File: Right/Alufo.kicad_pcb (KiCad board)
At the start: 2 copper layers, 139.7 x 88.9 mm, 67 parts, among them J2 USB_C_Receptacle_USB2.0_16P_2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, J4 USB_C_Receptacle_USB2.0_16P_2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, K11 PG1350, K12 PG1350, K13 PG1350, K14 PG1350, K15 PG1350, K16 PG1350, K21 PG1350, K22 PG1350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

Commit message: Manually add cutouts for 2010 resistors
Using middle-layer cutouts defined in the footprint no longer works as the resistors are now vertically aligned in relation to each rather than a set distance from the switch sockets.
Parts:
- R11, R12, R13, R14, R15: footprint Project Library:R_2010_5025Metric_Mod -> Resistor_SMD:R_2010_5025Metric
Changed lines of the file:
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@@
 		)
 	)
-	(footprint "Project Library:R_2010_5025Metric_Mod"
+	(footprint "Resistor_SMD:R_2010_5025Metric"
 		(layer "F.Cu")
 		(at 189.22 54.291679 -90)
@@
 		(tags "resistor")
 		(property "Reference" "R12"
-			(at 0 0 90)
+			(at 0 0 -90)
 			(layer "F.SilkS")
 			(effects
@@
 		)
 		(property "Value" "0R"
-			(at 0 2.28 90)
+			(at 0 2.28 -90)
 			(layer "F.Fab")
 			(effects
@@
 			)
 		)
-		(property "Footprint" "Project Library:R_2010_5025Metric_Mod"
+		(property "Footprint" "Resistor_SMD:R_2010_5025Metric"
 			(at 0 0 -90)
 			(unlocked yes)
@@
 			(layer "F.Fab")
 		)
-		(fp_rect
-			(start -9 -1.825)
-			(end 9 1.825)
-			(stroke
-				(width 0.1)
-				(type default)
-			)
-			(fill none)
-			(layer "User.1")
-		)
 		(fp_text user "${REFERENCE}"
-			(at 0 0 90)
+			(at 0 0 -90)
 			(layer "F.Fab")
 			(effects
@@
 		)
 	)
-	(footprint "Project Library:R_2010_5025Metric_Mod"
+	(footprint "Resistor_SMD:R_2010_5025Metric"
 		(layer "F.Cu")
 		(at 132.07 54.291679 -90)
@@
 			)
 		)
-		(property "Footprint" "Project Library:R_2010_5025Metric_Mod"
+		(property "Footprint" "Resistor_SMD:R_2010_5025Metric"
 			(at 0 0 -90)
 			(unlocked yes)
@@
 			(layer "F.Fab")
 		)
-		(fp_rect
-			(start -9 -1.825)
-			(end 9 1.825)
-			(stroke
-				(width 0.1)
-				(type default)
-			)
-			(fill none)
-			(layer "User.1")
-		)
 		(fp_text user "${REFERENCE}"
 			(at 0 0 -90)
@@
 		)
 	)
-	(footprint "Project Library:R_2010_5025Metric_Mod"
+	(footprint "Resistor_SMD:R_2010_5025Metric"
 		(layer "F.Cu")
 		(at 205.525 64.666681 -90)
@@
 			)
 		)
-		(property "Footprint" "Project Library:R_2010_5025Metric_Mod"
+		(property "Footprint" "Resistor_SMD:R_2010_5025Metric"
 			(at 0 0 -90)
 			(unlocked yes)
@@
 			(layer "F.Fab")
 		)
-		(fp_rect
-			(start -9 -1.825)
-			(end 9 1.825)
-			(stroke
-				(width 0.1)
-				(type default)
-			)
-			(fill none)
-			(layer "User.1")
-		)
 		(fp_text user "${REFERENCE}"
 			(at 0 0 -90)
@@
 		)
 	)
-	(footprint "Project Library:R_2010_5025Metric_Mod"
+	(footprint "Resistor_SMD:R_2010_5025Metric"
 		(layer "F.Cu")
 		(at 170.17 54.291679 -90)
@@
 			)
 		)
-		(property "Footprint" "Project Library:R_2010_5025Metric_Mod"
+		(property "Footprint" "Resistor_SMD:R_2010_5025Metric"
 			(at 0 0 -90)
 			(unlocked yes)
@@
 			(layer "F.Fab")
 		)
-		(fp_rect
-			(start -9 -1.825)
-			(end 9 1.825)
-			(stroke
-				(width 0.1)
-				(type default)
-			)
-			(fill none)
-			(layer "User.1")
-		)
 		(fp_text user "${REFERENCE}"
 			(at 0 0 -90)
@@
 		)
 	)
-	(footprint "Project Library:R_2010_5025Metric_Mod"
+	(footprint "Resistor_SMD:R_2010_5025Metric"
 		(layer "F.Cu")
 		(at 151.12 54.291679 -90)
@@
 			)
 		)
-		(property "Footprint" "Project Library:R_2010_5025Metric_Mod"
+		(property "Footprint" "Resistor_SMD:R_2010_5025Metric"
 			(at 0 0 -90)
 			(unlocked yes)
@@
 			(layer "F.Fab")
 		)
-		(fp_rect
-			(start -9 -1.825)
-			(end 9 1.825)
-			(stroke
-				(width 0.1)
-				(type default)
-			)
-			(fill none)
-			(layer "User.1")
-		)
 		(fp_text user "${REFERENCE}"
 			(at 0 0 -90)
@@
 		(layer "Edge.Cuts")
 	)
+	(gr_rect
+		(start 149.295 43.416676)
+		(end 152.945 60.41668)
+		(stroke
+			(width 0.1)
+			(type default)
+		)
+		(fill none)
+		(layer "User.1")
+	)
+	(gr_rect
+		(start 203.7 56.166679)
+		(end 207.35 73.166683)
+		(stroke
+			(width 0.1)
+			(type default)
+		)
+		(fill none)
+		(layer "User.1")
+	)
+	(gr_rect
+		(start 130.245 47.666677)
+		(end 133.895 57.785)
+		(stroke
+			(width 0.1)
+			(type default)
+		)
+		(fill none)
+		(layer "User.1")
+	)
+	(gr_rect
+		(start 168.345 50.8)
+		(end 171.995 60.41668)
+		(stroke
+			(width 0.1)
+			(type default)
+		)
+		(fill none)
+		(layer "User.1")
+	)
 	(gr_poly
 		(pts
@@
 		)
 		(fill none)
+		(layer "User.1")
+	)
+	(gr_rect
+		(start 187.395 47.666677)
+		(end 191.045 64.666681)
+		(stroke
+			(width 0.1)
+			(type default)
+		)
+		(fill none)

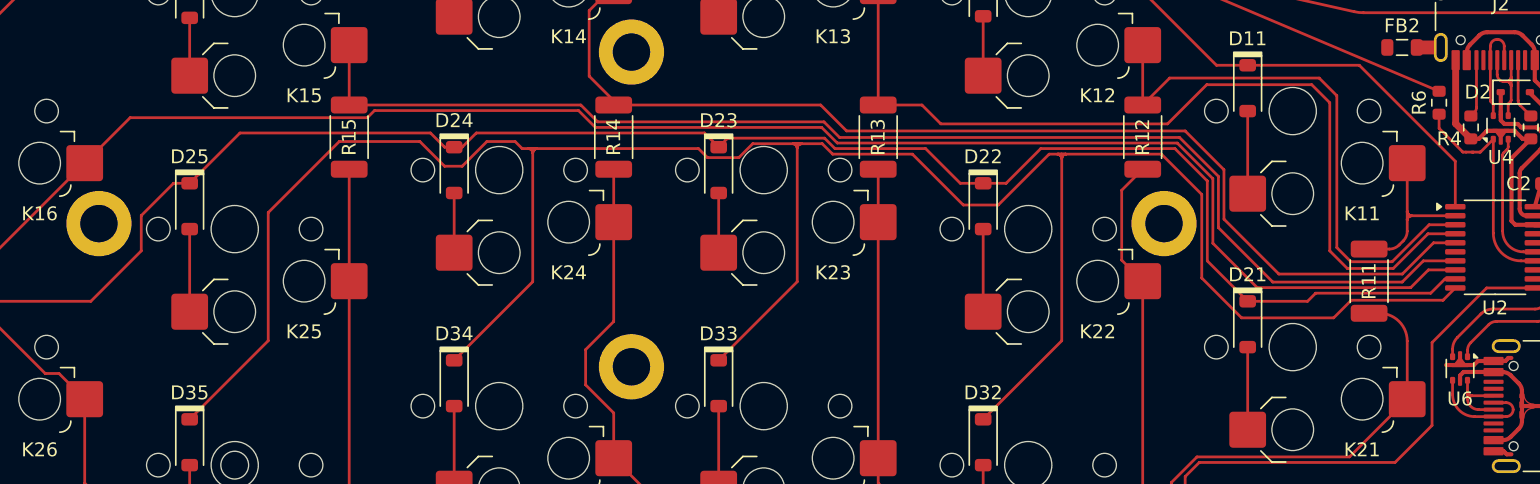
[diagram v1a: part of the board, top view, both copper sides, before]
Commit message: Clean up routing through jumper resistors
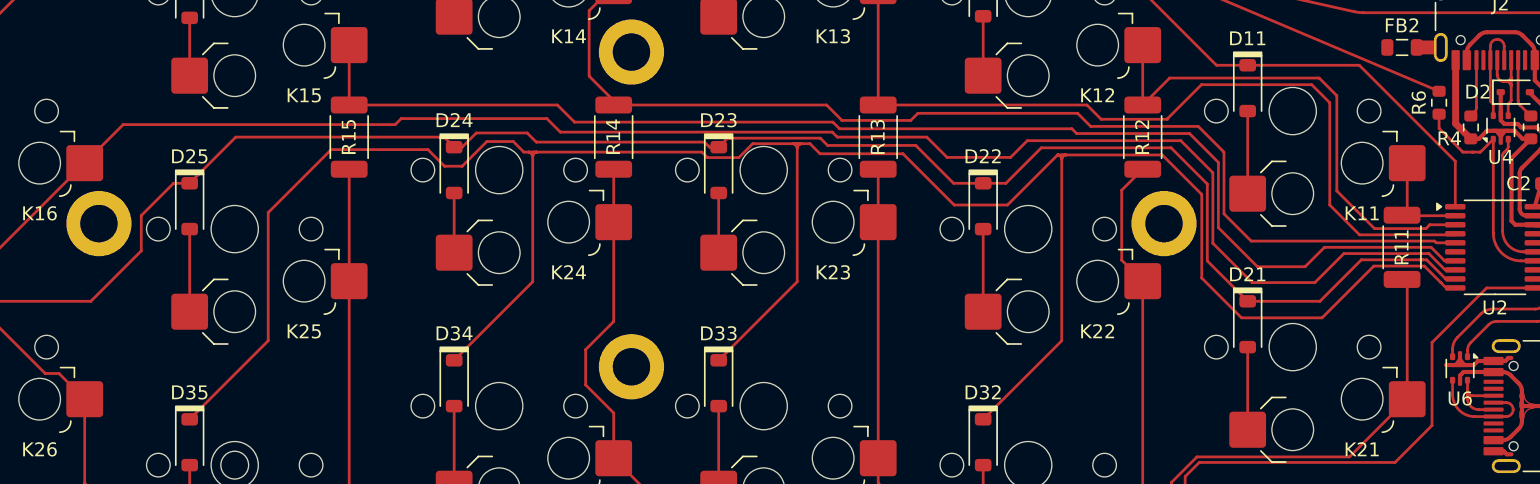
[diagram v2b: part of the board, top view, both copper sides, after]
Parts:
- moved R11 3.40 mm to (207.9, 62.2)
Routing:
- net Col2: track 40.6 -> 36.3 mm
- net Col3: track 64.6 -> 60.4 mm
- net Col1: track 10.9 -> 7.93 mm
- net Col6: track 249.6 -> 251.0 mm
- net Col1T: track 80.8 -> 82.2 mm
- net Row2: track 129.2 -> 130.3 mm
- net Col4: track 78.4 -> 77.5 mm
- net Row3: track 176.8 -> 176.2 mm

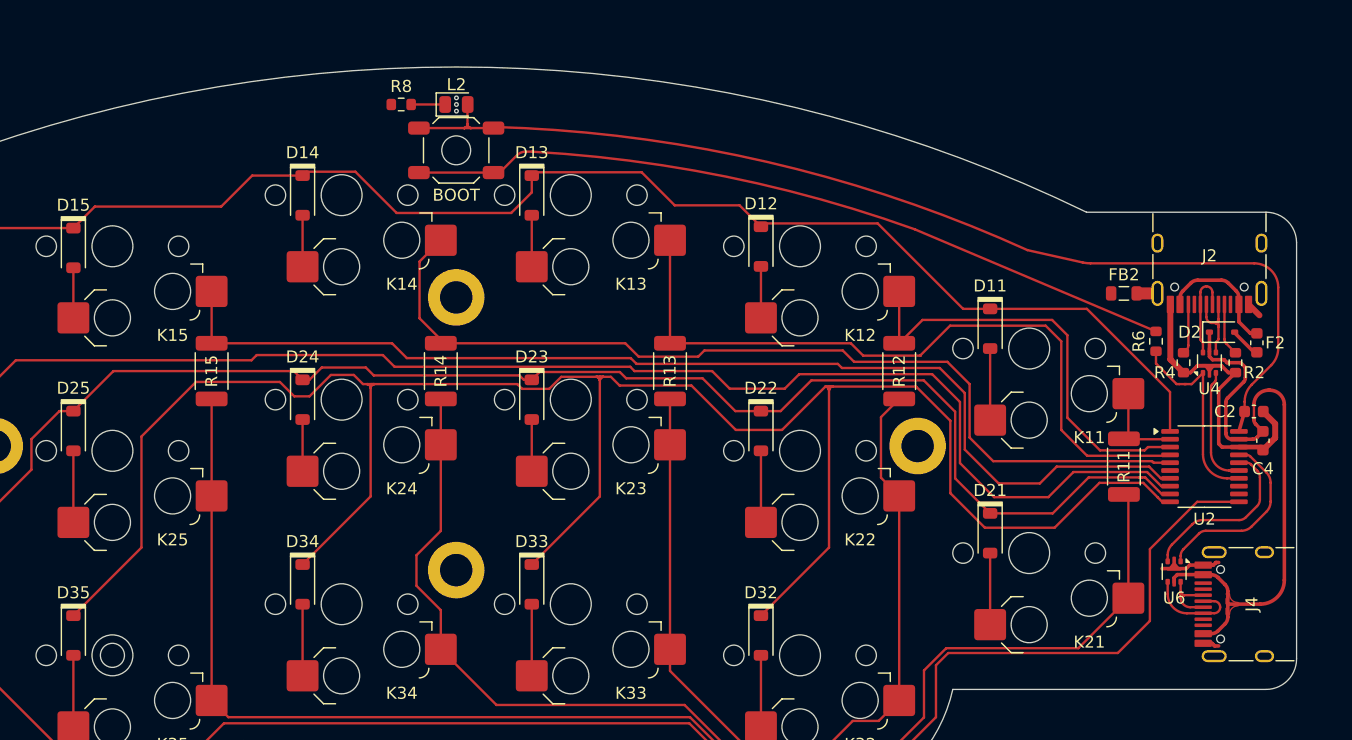
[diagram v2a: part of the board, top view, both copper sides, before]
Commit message: Move boot switch and tweak location of power LED
Boot switch is now closer to the MCU, roughly where the LED would be on the switches K15 (lefthand) or K12 (righthand). The power LED is now a little further away from the top edge.
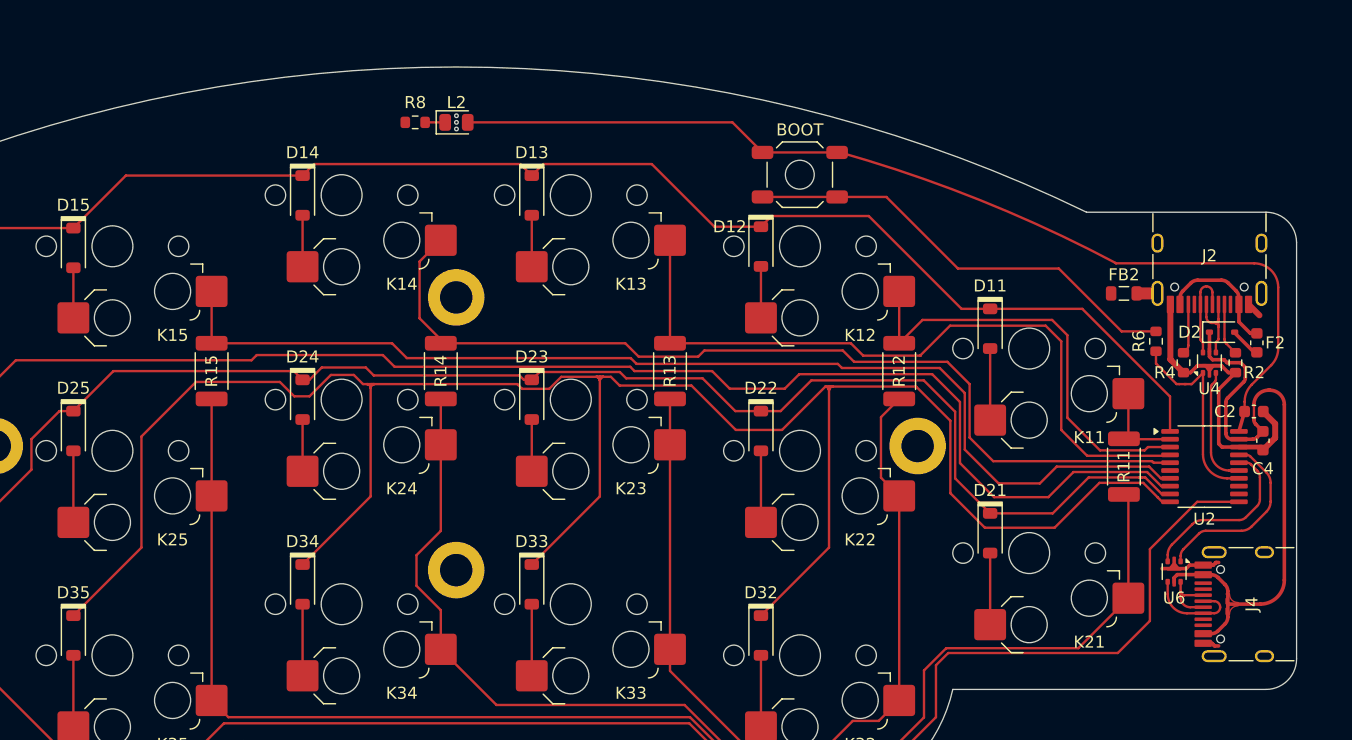
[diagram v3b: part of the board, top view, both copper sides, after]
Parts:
- moved SW2 28.6 mm to (181.0, 38.0)
- moved R8 1.89 mm to (149.0, 33.6)
- moved L2 1.49 mm to (152.4, 33.6)
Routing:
- net +3V3: track 42.3 -> 59.3 mm
- net BOOT: track 31.4 -> 37.3 mm
- net Net-(L2-K): track 2.96 -> 1.67 mm
- net Row1: track 129.1 -> 127.9 mm
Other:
- outline, holes or cut-outs redrawn

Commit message: Clean up routing of right thumb keys
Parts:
- moved D43 0.30 mm to (197.6, 100.7)
- moved D44 0.30 mm to (195.2, 100.2)
- moved D41 0.30 mm to (202.6, 101.6)
- moved D46 0.30 mm to (190.4, 99.2)
- moved D45 0.30 mm to (192.8, 99.7)
- moved D42 0.30 mm to (200.1, 101.1)
- renumbered D46 to D42, D42 to D43, D43 to D44, D44 to D46
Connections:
- D42 pad 1: Net-(D46-K) -> Net-(D42-K)
- D42 pad 2: Col6 -> Col2T
- D43 pad 1: Net-(D42-K) -> Net-(D43-K)
- D43 pad 2: Col2T -> Col3T
- D44 pad 1: Net-(D43-K) -> Net-(D44-K)
- D44 pad 2: Col3T -> Col4T
- D46 pad 1: Net-(D44-K) -> Net-(D46-K)
- D46 pad 2: Col4T -> Col6
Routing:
- net Net-(D46-K): track 40.5 -> 28.4 mm
- net Col6: track 251.0 -> 239.5 mm
- net Row4: track 172.3 -> 164.1 mm
- net Net-(D44-K): track 26.9 -> 32.4 mm
- net Col4T: track 72.8 -> 77.5 mm
- net Net-(D42-K): track 18.0 -> 22.1 mm
- net Col3T: track 58.2 -> 61.0 mm
- net Net-(D43-K): track 18.6 -> 17.4 mm
- net Col5T: track 96.0 -> 95.0 mm
- net Col2T: track 62.8 -> 63.4 mm

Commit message: Clean-up traces on righthand board
Also make tweaks to lefthand
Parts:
- moved NT2 0.26 mm to (212.7, 55.4)
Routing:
- net +3V3: track 59.3 -> 84.0 mm
- net Row3: track 176.2 -> 186.0 mm
- net Row1: track 127.9 -> 123.9 mm
- net Col1T: track 82.5 -> 79.6 mm
- net Row4: track 164.1 -> 161.3 mm
- net BOOT: track 37.3 -> 35.2 mm
- net Col5T: track 95.0 -> 93.5 mm
- net Col4T: track 77.5 -> 76.1 mm
- net Col5: track 92.5 -> 93.9 mm
- net Net-(D42-K): track 22.1 -> 20.7 mm
- net Col2T: track 63.4 -> 62.2 mm
- net Row2: track 130.3 -> 129.3 mm
- net Col3T: track 61.0 -> 60.0 mm

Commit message: Minor tweaks
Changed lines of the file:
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@@
-	)
-	(segment
-		(start 215.408 53.344008)
-		(end 216.23265 53.344008)
-		(width 0.3)
-		(layer "F.Cu")
-		(net 21)
-	)
-	(segment
-		(start 216.7144 59.955)
-		(end 216.8705 59.955)
-		(width 0.3)
-		(layer "F.Cu")
-		(net 21)
 	)
 	(segment
@@
 	)
 	(segment
-		(start 216.23265 53.344008)
-		(end 216.424064 53.535422)
-		(width 0.3)
-		(layer "F.Cu")
-		(net 21)
-	)
-	(segment
 		(start 215.722315 71.450999)
 		(end 216.300686 72.02937)
@@
 		(start 212.074 71.882)
 		(end 212.074 71.464344)
-		(width 0.3)
-		(layer "F.Cu")
-		(net 21)
-	)
-	(segment
-		(start 216.424064 53.535422)
-		(end 217.54478 53.535422)
 		(width 0.3)
 		(layer "F.Cu")
@@
 	)
 	(segment
+		(start 216.506907 53.535422)
+		(end 217.337673 53.535422)
+		(width 0.3)
+		(layer "F.Cu")
+		(net 21)
+	)
+	(segment
+		(start 217.691227 53.681869)
+		(end 217.848554 53.839196)
+		(width 0.3)
+		(layer "F.Cu")
+		(net 21)
+	)
+	(segment
+		(start 216.291229 53.402587)
+		(end 216.365486 53.476844)
+		(width 0.3)
+		(layer "F.Cu")
+		(net 21)
+	)
+	(segment
+		(start 218.705999 58.347892)
+		(end 218.705999 58.166)
+		(width 0.3)
+		(layer "F.Cu")
+		(net 21)
+	)
+	(segment
+		(start 216.300685 75.303999)
+		(end 215.722314 75.88237)
+		(width 0.3)
+		(layer "F.Cu")
+		(net 21)
+	)
+	(segment
+		(start 219.905999 55.88)
+		(end 220.034 55.88)
+		(width 0.3)
+		(layer "F.Cu")
+		(net 21)
+	)
+	(segment
+		(start 217.458 59.955)
+		(end 218.598893 59.955)
+		(width 0.3)
+		(layer "F.Cu")
+		(net 21)
+	)
+	(segment
+		(start 217.995 54.192749)
+		(end 217.995 54.991376)
+		(width 0.3)
+		(layer "F.Cu")
+		(net 21)
+	)
+	(segment
+		(start 215.408 53.344008)
+		(end 216.149807 53.344008)
+		(width 0.3)
+		(layer "F.Cu")
+		(net 21)
+	)
+	(segment
+		(start 216.3705 57.03009)
+		(end 216.3705 59.403993)
+		(width 0.3)
+		(layer "F.Cu")
+		(net 21)
+	)
+	(segment
+		(start 216.516947 59.757547)
+		(end 216.567954 59.808554)
+		(width 0.3)
+		(layer "F.Cu")
+		(net 21)
+	)
+	(segment
+		(start 217.848553 55.34493)
+		(end 216.516946 56.676537)
+		(width 0.3)
+		(layer "F.Cu")
+		(net 21)
+	)
+	(segment
+		(start 216.921507 59.955)
+		(end 217.458 59.955)
+		(width 0.3)
+		(layer "F.Cu")
+		(net 21)
+	)
+	(segment
 		(start 215.008 52.669)
 		(end 215.008 52.944008)
-		(width 0.3)
-		(layer "F.Cu")
-		(net 21)
-	)
-	(segment
-		(start 218.705999 58.347892)
-		(end 218.705999 58.166)
-		(width 0.3)
-		(layer "F.Cu")
-		(net 21)
-	)
-	(segment
-		(start 216.300685 75.303999)
-		(end 215.722314 75.88237)
-		(width 0.3)
-		(layer "F.Cu")
-		(net 21)
-	)
-	(segment
-		(start 217.54478 53.535422)
-		(end 217.995 53.985642)
-		(width 0.3)
-		(layer "F.Cu")
-		(net 21)
-	)
-	(segment
-		(start 216.3705 56.822983)
-		(end 216.3705 59.6111)
-		(width 0.3)
-		(layer "F.Cu")
-		(net 21)
-	)
-	(segment
-		(start 216.3705 59.6111)
-		(end 216.7144 59.955)
-		(width 0.3)
-		(layer "F.Cu")
-		(net 21)
-	)
-	(segment
-		(start 217.995 53.985642)
-		(end 217.995 55.198483)
-		(width 0.3)
-		(layer "F.Cu")
-		(net 21)
-	)
-	(segment
-		(start 219.905999 55.88)
-		(end 220.034 55.88)
-		(width 0.3)
-		(layer "F.Cu")
-		(net 21)
-	)
-	(segment
-		(start 217.458 59.955)
-		(end 218.598893 59.955)
-		(width 0.3)
-		(layer "F.Cu")
-		(net 21)
-	)
-	(segment
-		(start 217.995 55.198483)
-		(end 216.3705 56.822983)
 		(width 0.3)
 		(layer "F.Cu")
@@
 	)
 	(arc
+		(start 216.365486 53.476844)
+		(mid 216.430371 53.520198)
+		(end 216.506907 53.535422)
+		(width 0.3)
+		(layer "F.Cu")
+		(net 21)
+	)
+	(arc
 		(start 215.722314 75.88237)
 		(mid 215.462775 76.055788)
@@
 	)
 	(arc
+		(start 216.149807 53.344008)
+		(mid 216.226344 53.359232)
+		(end 216.291229 53.402587)
+		(width 0.3)
+		(layer "F.Cu")
+		(net 21)
+	)
+	(arc
+		(start 217.337673 53.535422)
+		(mid 217.529015 53.573482)
+		(end 217.691227 53.681869)
+		(width 0.3)
+		(layer "F.Cu")
+		(net 21)
+	)
+	(arc
 		(start 216.535 74.738313)
 		(mid 216.474103 75.04446)
@@
 	)
 	(arc
+		(start 216.3705 57.03009)
+		(mid 216.40856 56.838749)
+		(end 216.516946 56.676537)
+		(width 0.3)
+		(layer "F.Cu")
+		(net 21)
+	)
+	(arc
 		(start 216.535 72.595055)
 		(mid 216.474104 72.288909)
@@
 	)
 	(arc
+		(start 217.995 54.991376)
+		(mid 217.95694 55.182718)
+		(end 217.848553 55.34493)
+		(width 0.3)
+		(layer "F.Cu")
+		(net 21)
+	)
+	(arc
+		(start 215.008 52.944008)
+		(mid 215.125157 53.226851)
+		(end 215.408 53.344008)
+		(width 0.3)
+		(layer "F.Cu")
+		(net 21)
+	)
+	(arc
 		(start 218.952447 59.808553)
 		(mid 218.790235 59.91694)
@@
 	)
 	(arc
-		(start 215.408 53.344008)
-		(mid 215.125157 53.226851)
-		(end 215.008 52.944008)
-		(width 0.3)
-		(layer "F.Cu")
+		(start 216.516947 59.757547)
+		(mid 216.40856 59.595335)
+		(end 216.3705 59.403993)
+		(width 0.3)
+		(layer "F.Cu")
+		(net 21)
+	)
+	(arc
+		(start 217.995 54.192749)
+		(mid 217.95694 54.001408)
+		(end 217.848554 53.839196)
+		(width 0.3)
+		(layer "F.Cu")
+		(net 21)
+	)
+	(arc
+		(start 216.567954 59.808554)
+		(mid 216.730166 59.91694)
+		(end 216.921507 59.955)
+		(width 0.3)
+		(layer "F.Cu")

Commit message: Further routing tweaks
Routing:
- net Col5T: track 93.5 -> 92.0 mm
- net Col2T: track 62.2 -> 60.8 mm
- net Col4: track 77.6 -> 76.4 mm
- net Col2: track 36.2 -> 35.2 mm
- net VCC: track 52.2 -> 51.6 mm
